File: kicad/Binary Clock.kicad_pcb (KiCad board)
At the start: 2 copper layers, 172.7 x 111.8 mm, 63 parts, among them J1 AVR-ISP-10, J2 UART, J3 COM/TW, SW1 INC_HOUR, SW2 INC_MINUTE, SW3 INC_SECOND, SW4 INC_BTNESS, U1 ATmega32A-PU, U2 PCF8583P, Y1 32768hZ

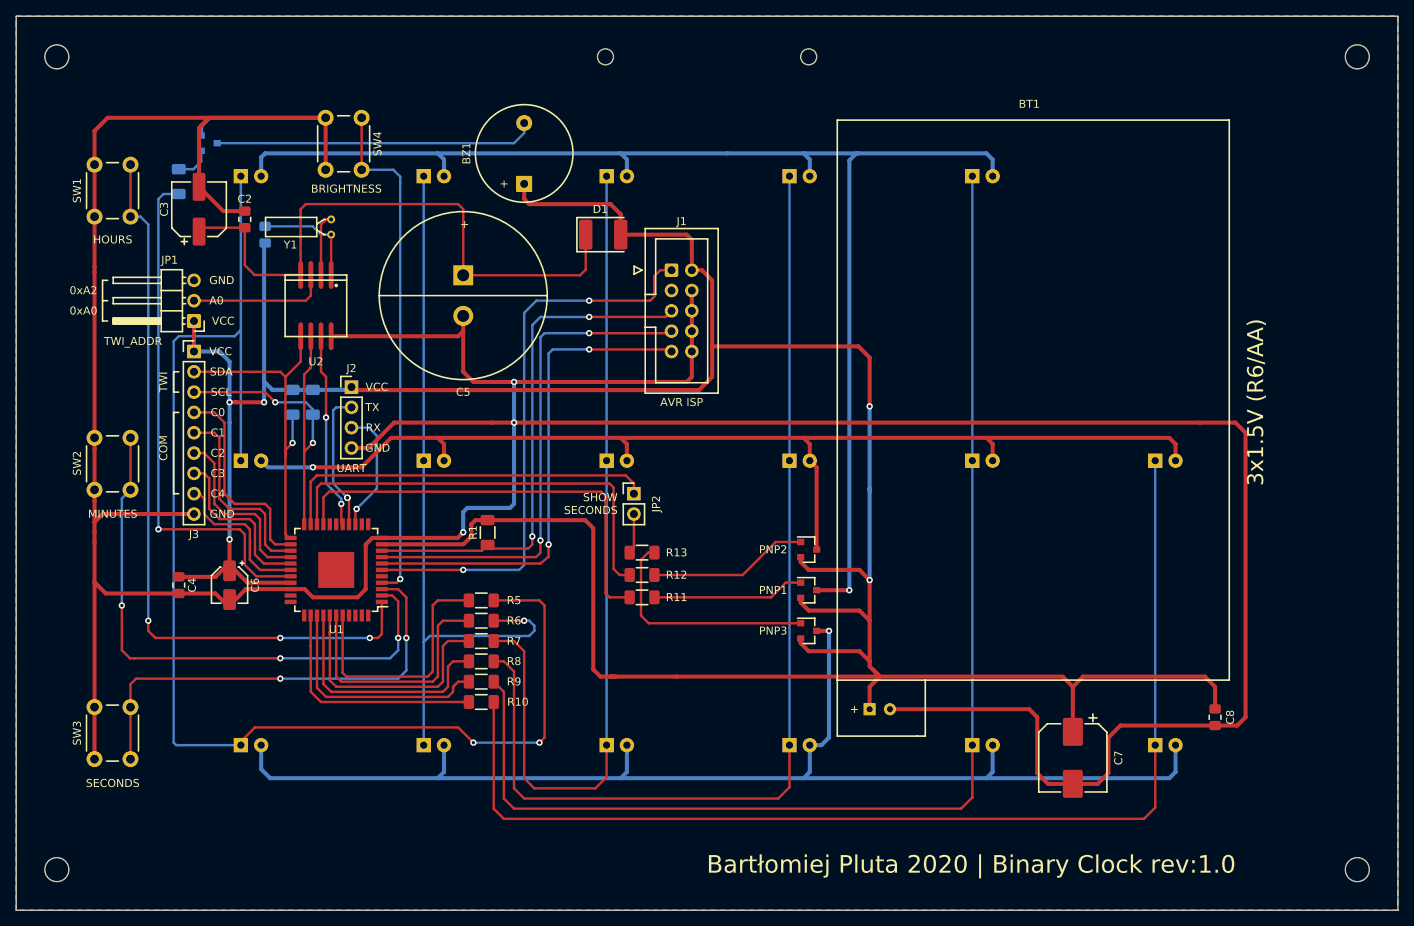
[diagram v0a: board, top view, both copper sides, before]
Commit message: Fix invalid ATmega footprint
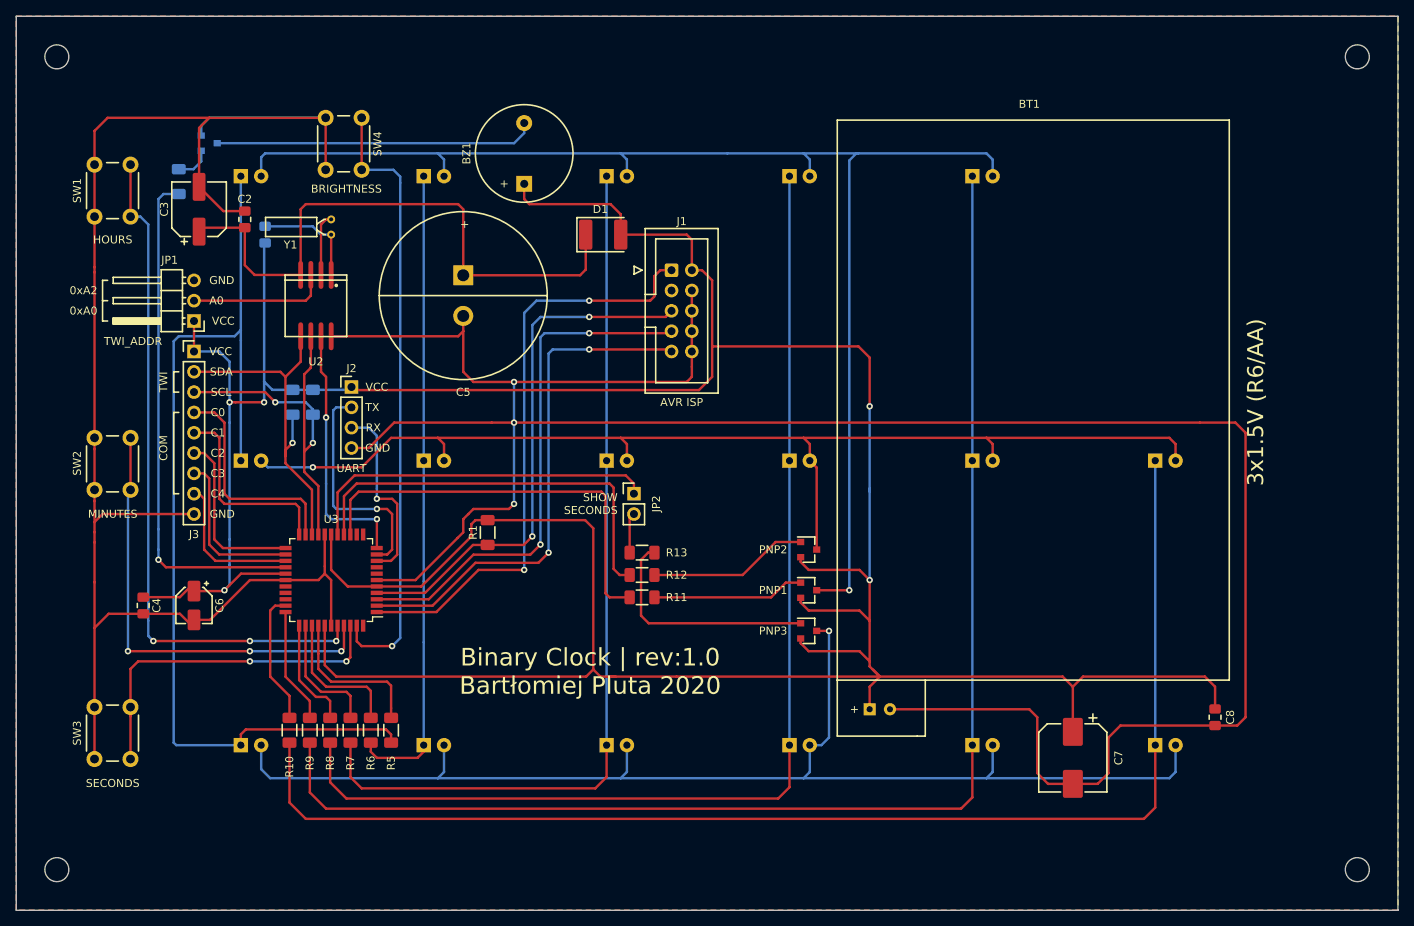
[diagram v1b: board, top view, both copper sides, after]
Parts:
- removed the REF** at (160.0, 55.9)
- removed the REF** at (134.6, 55.9)
- removed U1: ATmega32A-PU, Package_QFP:TQFP-44-1EP_10x10mm_P0.8mm_EP4.5x4.5mm
- added U3: ATmega32-16AU, Package_QFP:TQFP-44_10x10mm_P0.8mm, F.Cu at (100.3, 121.3)
- moved R10 24.2 mm to (95.1, 140.1), turned to 90 degrees
- moved R9 22.3 mm to (97.7, 140.1), turned to 90 degrees
- moved R8 20.8 mm to (100.2, 140.1), turned to 90 degrees
- moved R7 19.8 mm to (102.7, 140.1), turned to 90 degrees
- moved R5 19.8 mm to (107.8, 140.1), turned to 90 degrees
- moved R6 19.5 mm to (105.3, 140.1), turned to 90 degrees
- moved C4 5.12 mm to (76.8, 124.5)
- moved C6 5.12 mm to (83.2, 124.5)
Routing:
- net VCC: track 409.7 -> 470.2 mm
- net Net-(HD1-Pad1): track 167.4 -> 125.5 mm, vias 2 -> 0
- net Net-(MD6-Pad1): track 140.5 -> 160.5 mm
- net /LED3: track 30.2 -> 13.9 mm
- net /LED4: track 30.4 -> 14.5 mm
- net Net-(HD5-Pad1): track 152.5 -> 168.1 mm
- net /LED2: track 31.1 -> 15.7 mm
- net /LED5: track 30.8 -> 16.6 mm
- net /INC_MINUTE: track 70.8 -> 56.8 mm
- net /INC_SECOND: track 57.2 -> 43.3 mm
- net /LED1: track 31.4 -> 17.5 mm
- net /INC_BTNESS: track 64.5 -> 77.4 mm
- net /LED0: track 31.9 -> 19.9 mm
- net /TX: track 17.5 -> 28.8 mm, vias 2 -> 1
- net Net-(HD2-Pad1): track 91.5 -> 80.3 mm, vias 1 -> 0
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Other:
- board text added: "Binary Clock | rev:1.0 Bartłomiej Pluta 2020"
- board text removed: "Bartłomiej Pluta 2020 | Binary Clock rev:1.0"

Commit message: Improve schema
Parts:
- J3: value COM/TW -> COM/TWI
- renumbered U3 to U1
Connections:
- net /COM0 renamed /C0
- net /COM1 renamed /C1
- net /COM2 renamed /C2
- net /COM3 renamed /C3
- net /COM4 renamed /C4
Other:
- board text added: "Binary Clock | rev: v1.0 Bartłomiej Pluta 2020"
- board text added: "VCAP"
- board text removed: "Binary Clock | rev:1.0 Bartłomiej Pluta 2020"
